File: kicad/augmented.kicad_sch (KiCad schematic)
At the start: 0 parts

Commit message: feat: preliminary wiring for pcb
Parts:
- added C10, C11, C12, C13, C14, C15, C16, C2, C6, C7, C9: 100nF, Capacitor_SMD:C_0603_1608Metric, symbol Device:C_Small
- added C17, C18: 15pF, Capacitor_SMD:C_0603_1608Metric, symbol Device:C_Small
- added C19, C20: 1uF, Capacitor_SMD:C_0603_1608Metric, symbol Device:C_Small
- added C5, C8: 10uF, Capacitor_SMD:C_0603_1608Metric, symbol Device:C_Small
- added D2, D3: WHITE, symbol Device:LED_Small
- added J1: USB_C_Receptacle_USB2.0_14P, symbol Connector:USB_C_Receptacle_USB2.0_14P
- added J2: Conn_01x04, Connector_JST:JST_GH_SM04B-GHS-TB_1x04-1MP_P1.25mm_Horizontal, symbol Connector_Generic:Conn_01x04
- added J3, J4: Conn_01x07, Connector_FFC-FPC:TE_0-1734839-7_1x07-1MP_P0.5mm_Horizontal, symbol Connector_Generic:Conn_01x07
- added R11, R5, R6: 1k, Resistor_SMD:R_0603_1608Metric, symbol Device:R_Small
- added R12: DNP, Resistor_SMD:R_0603_1608Metric, symbol Device:R_Small
- added R3, R4: 5.1k, Resistor_SMD:R_0603_1608Metric, symbol Device:R_Small
- added R7, R8: 27, Resistor_SMD:R_0603_1608Metric, symbol Device:R_Small
- added SW1: RESET, Button_Switch_SMD:SW_SPST_SKQG_WithoutStem, symbol Switch:SW_SPST
- added SW2: BOOT, Button_Switch_SMD:SW_SPST_SKQG_WithoutStem, symbol Switch:SW_SPST
- added U1: USBLC6-2P6, Package_TO_SOT_SMD:SOT-666, symbol Power_Protection:USBLC6-2P6
- added U2: RP2040, Package_DFN_QFN:QFN-56-1EP_7x7mm_P0.4mm_EP3.2x3.2mm, symbol MCU_RaspberryPi:RP2040
- added U3: NCP1117-3.3_SOT223, Package_TO_SOT_SMD:SOT-223-3_TabPin2, symbol Regulator_Linear:NCP1117-3.3_SOT223
- added U5: W25Q128JVS, Package_SO:SOIC-8_5.3x5.3mm_P1.27mm, symbol Memory_Flash:W25Q128JVS
- added Y1: 12MHz, Crystal:Crystal_SMD_Abracon_ABM8AIG-4Pin_3.2x2.5mm, symbol Device:Crystal_GND24
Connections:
- new net: C2.2, U1.5 (VBUS)
- new net: J1.A5 (CC1), R3.1
- new net: J1.B5 (CC2), R4.1
- new net: R7.2, U2.46 (USB_DM)
- new net: R8.2, U2.47 (USB_DP)
- new net: R11.1, SW2.1 (A)
- new net +1V1: C14.1, C15.1, C19.1, U2.23 (DVDD), U2.45 (VREG_VOUT), U2.50 (DVDD)
- new net +3V3: C10.1, C11.1, C12.1, C13.1, C16.1, C20.1, C6.1, C7.1, C8.1, C9.1, R12.1, R5.1, R6.1, U2.1 (IOVDD), U2.10 (IOVDD), U2.22 (IOVDD), U2.33 (IOVDD), U2.42 (IOVDD), U2.43 (ADC_AVDD), U2.44 (VREG_VIN), U2.48 (USB_VDD), U2.49 (IOVDD), U3.2 (VO), U5.8 (VCC)
- new net +5V: C2.1, C5.1, J1.A4 (VBUS), J1.A9 (VBUS), J1.B4 (VBUS), J1.B9 (VBUS), J2.1 (Pin_1), U3.3 (VI)
- new net COL0: J3.5 (Pin_5), J4.4 (Pin_4), U2.41 (GPIO29/ADC3)
- new net COL1: J3.4 (Pin_4), J4.3 (Pin_3), U2.40 (GPIO28/ADC2)
- new net COL10: U2.16 (GPIO13)
- new net COL11: U2.15 (GPIO12)
- new net COL12: U2.14 (GPIO11)
- new net COL13: U2.13 (GPIO10)
- new net COL14: U2.2 (GPIO0)
- new net COL15: U2.5 (GPIO3)
- new net COL16: U2.7 (GPIO5)
- new net COL2: U2.39 (GPIO27/ADC1)
- new net COL3: U2.38 (GPIO26/ADC0)
- new net COL4: U2.37 (GPIO25)
- new net COL5: U2.36 (GPIO24)
- new net COL6: U2.35 (GPIO23)
- new net COL7: U2.34 (GPIO22)
- new net COL8: U2.18 (GPIO15)
- new net COL9: U2.17 (GPIO14)
- new net D+: J1.A6 (D+), J1.B6 (D+), U1.3 (I/O2)
- new net D-: J1.A7 (D-), J1.B7 (D-), U1.1 (I/O1)
- new net GND: C10.2, C11.2, C12.2, C13.2, C14.2, C15.2, C16.2, C17.1, C18.1, C19.2, C20.2, C5.2, C6.2, C7.2, C8.2, C9.2, D2.1 (K), D3.1 (K), J1.A1 (GND), J1.A12 (GND), J1.B1 (GND), J1.B12 (GND), J1.SH (SHIELD), J2.4 (Pin_4), R3.2, R4.2, SW1.2 (B), SW2.2 (B), U1.2 (GND), U2.57 (GND), U3.1 (GND), U5.4 (GND), Y1.2 (G), Y1.4 (G)
- new net LED_CAPS: D3.2 (A), R6.2
- new net PWR_LED: D2.2 (A), R5.2
- new net QSPI_CLK: U2.52 (QSPI_SCLK), U5.6 (CLK)
- new net QSPI_SD0: U2.53 (QSPI_SD0), U5.5 (DI/IO_{0})
- new net QSPI_SD1: U2.55 (QSPI_SD1), U5.2 (DO/IO_{1})
- new net QSPI_SD2: U2.54 (QSPI_SD2), U5.3 (~{WP}/IO_{2})
- new net QSPI_SD3: U2.51 (QSPI_SD3), U5.7 (~{HOLD}/~{RESET}/IO_{3})
- new net QSPI_SS: R11.2, R12.2, U2.56 (~{QSPI_SS}), U5.1 (~{CS})
- new net RESET: SW1.1 (A), U2.26 (RUN)
- new net ROW0: J3.2 (Pin_2), J4.7 (Pin_7), U2.8 (GPIO6)
- new net ROW1: J3.1 (Pin_1), J4.6 (Pin_6), U2.6 (GPIO4)
- new net ROW2: J3.3 (Pin_3), J4.5 (Pin_5), U2.4 (GPIO2)
- new net ROW3: J3.7 (Pin_7), J4.1 (Pin_1), U2.3 (GPIO1)
- new net ROW4: J3.6 (Pin_6), J4.2 (Pin_2), U2.28 (GPIO17)
- new net USB_D+: J2.3 (Pin_3), R8.1, U1.4 (I/O2)
- new net USB_D-: J2.2 (Pin_2), R7.1, U1.6 (I/O1)
- new net XIN: C18.2, U2.20 (XIN), Y1.1
- new net XOUT: C17.2, U2.21 (XOUT), Y1.3
- no-connect marks 0 -> 11
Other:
- added sheet Keyboard Matrix (matrix.kicad_sch)
- note added: "*Pin 44"
- note added: "*Pin 45"

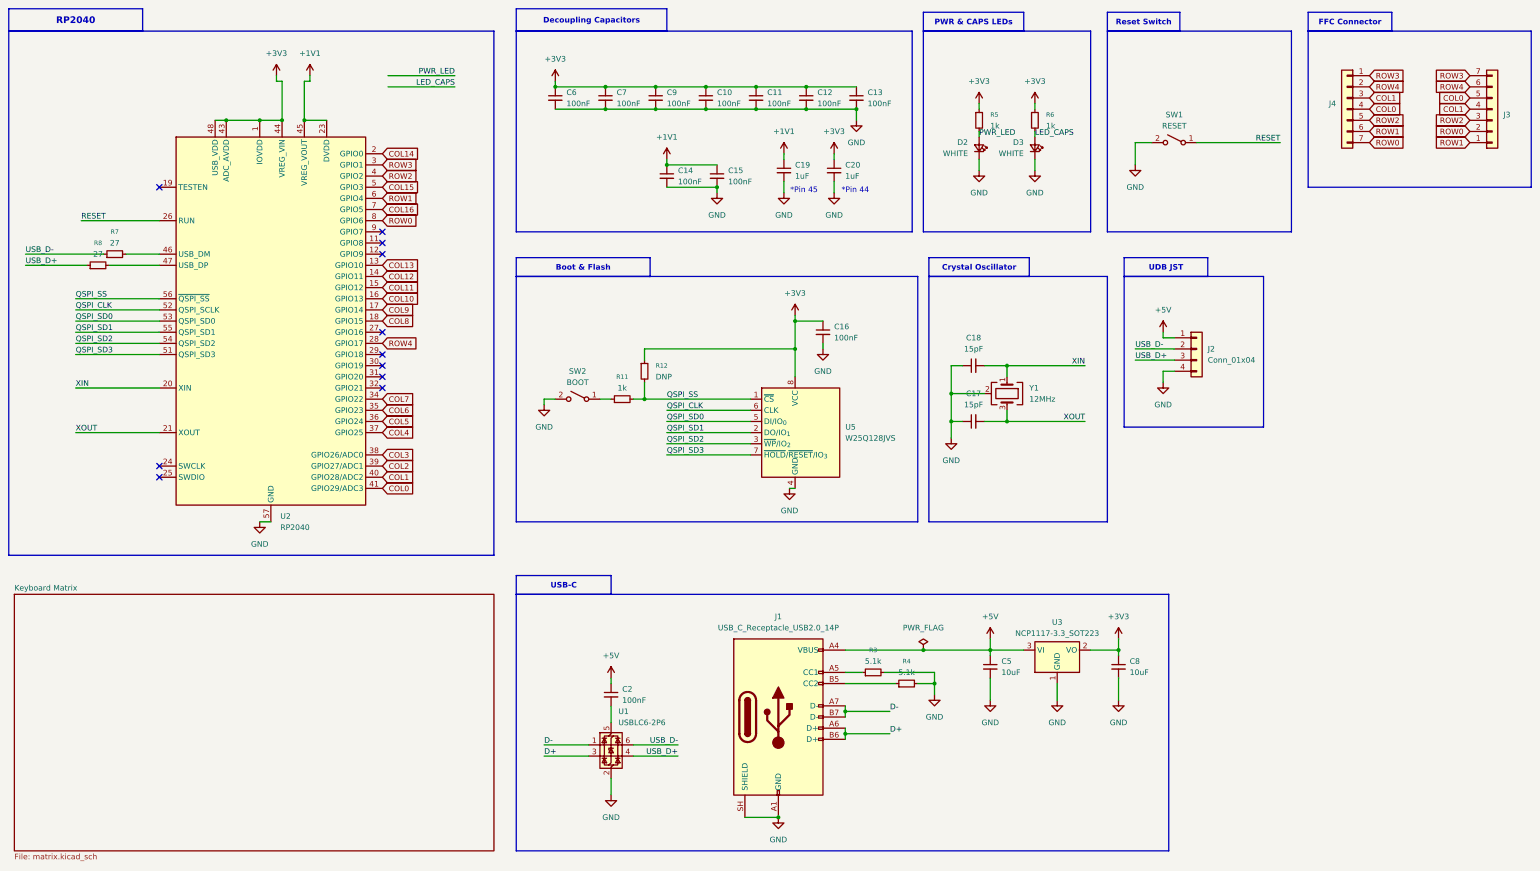
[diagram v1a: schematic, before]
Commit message: feat: add daughterboard pcb
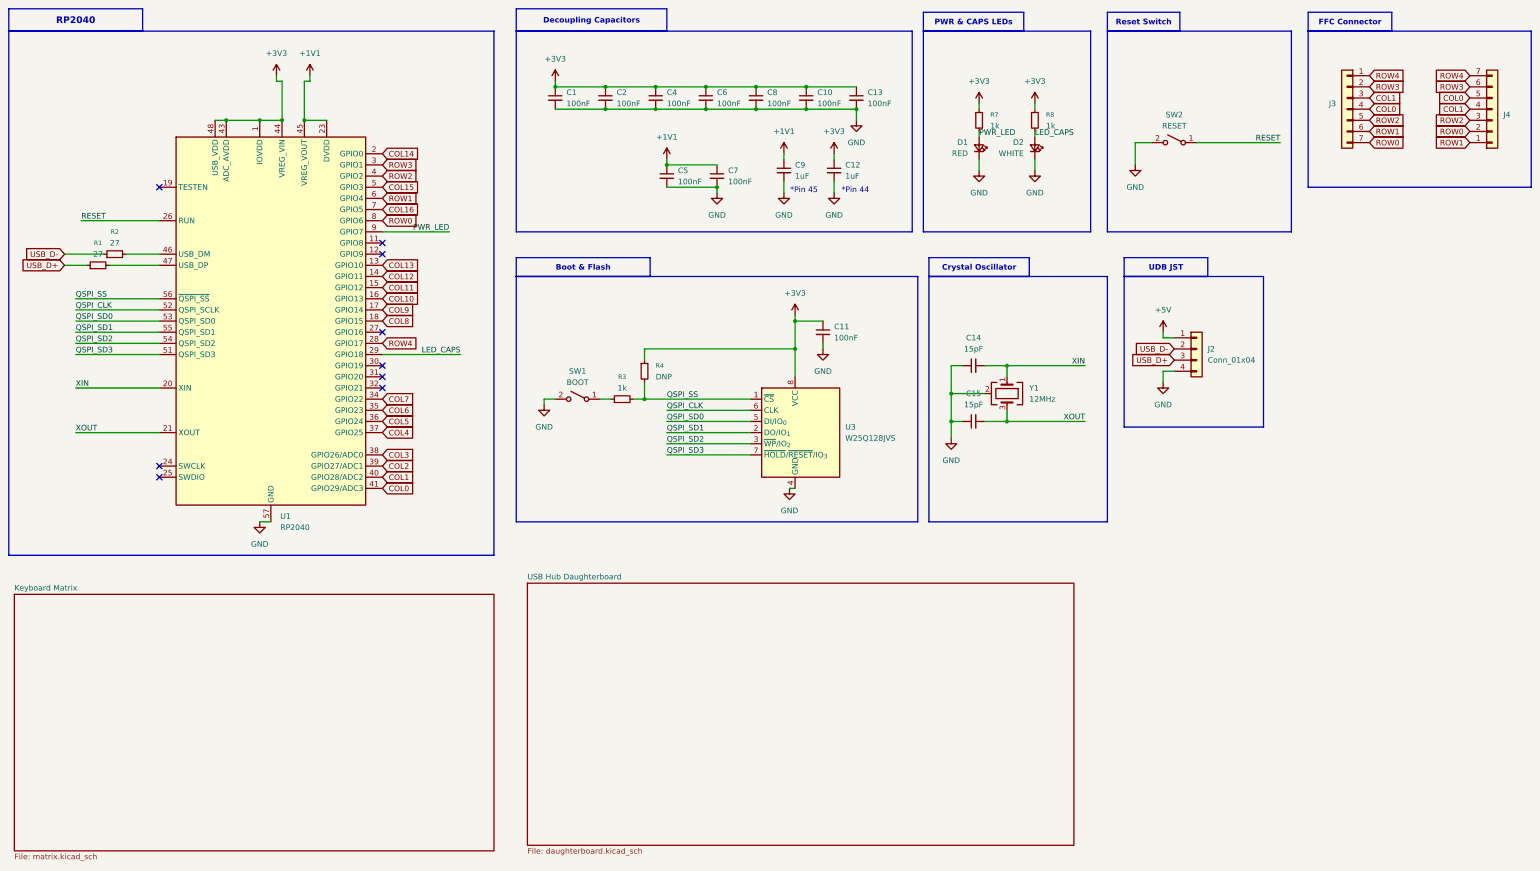
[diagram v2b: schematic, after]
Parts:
- removed C2: 100nF, Capacitor_SMD:C_0603_1608Metric, symbol Device:C_Small
- removed C5, C8: 10uF, Capacitor_SMD:C_0603_1608Metric, symbol Device:C_Small
- removed J1: USB_C_Receptacle_USB2.0_14P, symbol Connector:USB_C_Receptacle_USB2.0_14P
- removed R3, R4: 5.1k, Resistor_SMD:R_0603_1608Metric, symbol Device:R_Small
- removed U1: USBLC6-2P6, Package_TO_SOT_SMD:SOT-666, symbol Power_Protection:USBLC6-2P6
- removed U3: NCP1117-3.3_SOT223, Package_TO_SOT_SMD:SOT-223-3_TabPin2, symbol Regulator_Linear:NCP1117-3.3_SOT223
- D1: renamed from D2; value WHITE -> RED; footprint (none) -> LED_SMD:LED_miniPLCC_2315_Handsoldering
- D2: renamed from D3; footprint (none) -> LED_SMD:LED_miniPLCC_2315_Handsoldering
- renumbered C6 to C1, C12 to C10, C16 to C11, C20 to C12, C18 to C14, C17 to C15, C7 to C2, C9 to C4, C14 to C5, C10 to C6, C15 to C7, C11 to C8, C19 to C9, J4 to J3, J3 to J4, R8 to R1, R7 to R2, R11 to R3, R12 to R4, R5 to R7, R6 to R8, SW2 to SW1, SW1 to SW2, U2 to U1, U5 to U3
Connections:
- net LED_CAPS: now also U1.29 (GPIO18)
- net PWR_LED: now also U1.9 (GPIO7)
- net ROW3: now also J3.2 (Pin_2), J4.6 (Pin_6); no longer J3.1 (Pin_1), J4.7 (Pin_7)
- net ROW4: now also J3.1 (Pin_1), J4.7 (Pin_7); no longer J3.2 (Pin_2), J4.6 (Pin_6)
- no-connect marks 11 -> 9
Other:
- added sheet USB Hub Daughterboard (daughterboard.kicad_sch)
